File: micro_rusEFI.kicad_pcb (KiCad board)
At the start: 2 copper layers, 80.6 x 93.7 mm, 172 parts, among them J1 USB_B_Micro, J19 Conn_01x06, J2 Conn_02x05_Odd_Even, J7 TC2030, SW1 SW_Push, SW2 SW_Push, SW3 SW_Push, SW4 SW_Push, U1 STM32F427VGT6, U2 LMR14020, U3 molex_48pin_MRE, U35 MCP6004, U36 MCP6004, U46 MCP6004, U5 LM1117-3.3, U8 MCP6004, X1 8MHz 20pF, Y2 32768 Hz

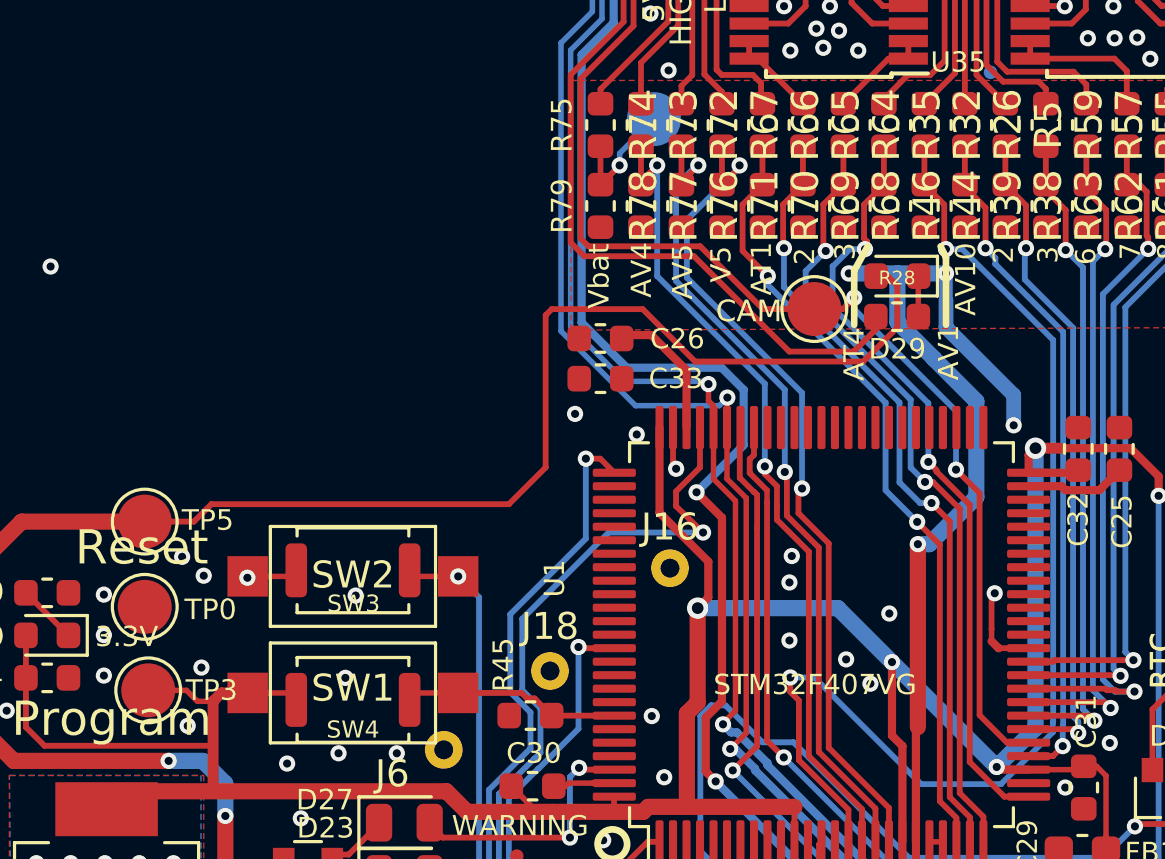
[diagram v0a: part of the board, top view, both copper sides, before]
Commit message: Added CAN x2
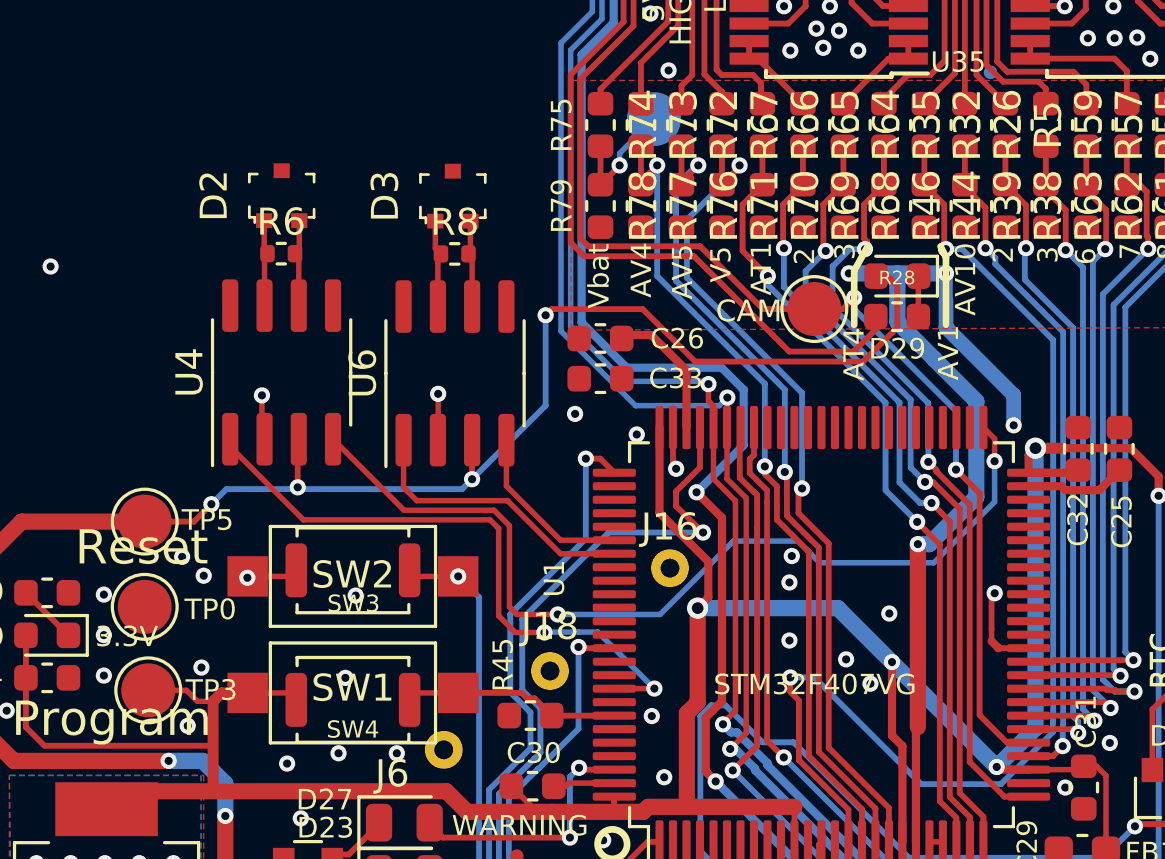
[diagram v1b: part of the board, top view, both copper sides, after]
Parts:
- added D2: PESD1CAN-UX, digikey-footprints:SOT-323, F.Cu at (34.1, 70.0)
- added D3: PESD1CAN-UX, digikey-footprints:SOT-323, F.Cu at (40.4, 70.0)
- added R6: 120, Resistor_SMD:R_0402_1005Metric, F.Cu at (34.1, 72.2)
- added R8: 120, Resistor_SMD:R_0402_1005Metric, F.Cu at (40.5, 72.2)
- added U4: TJA1051T-3, Package_SO:SOIC-8_3.9x4.9mm_P1.27mm, F.Cu at (34.1, 76.6)
- added U6: TJA1051T-3, Package_SO:SOIC-8_3.9x4.9mm_P1.27mm, F.Cu at (40.5, 76.6)
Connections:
- U1 pad 51: /MCU/PB12 -> /CAN Transceiver/RXDCAN1
- U1 pad 81: /MCU/PD0 -> /CAN Transceiver/RXDCAN2
- U1 pad 82: /MCU/PD1 -> /CAN Transceiver/TXDCAN2
- U1 pad 92: /MCU/PB6 -> /CAN Transceiver/TXDCAN1
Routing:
- net /CAN Transceiver/RXDCAN1: track 0.00 -> 34.3 mm, vias 0 -> 2
- net /CAN Transceiver/TXDCAN1: track 0.00 -> 23.1 mm, vias 0 -> 2
- net /CAN Transceiver/TXDCAN2: track 0.00 -> 10.6 mm
- net /CAN Transceiver/RXDCAN2: track 0.00 -> 6.53 mm
- net GND: track 116.4 -> 119.9 mm, vias 234 -> 236
- net Net-(D3-Pad1): track 0.00 -> 3.30 mm
- net Net-(D2-Pad2): track 0.00 -> 3.27 mm
- net Net-(D3-Pad2): track 0.00 -> 3.25 mm
- net Net-(D2-Pad1): track 0.00 -> 3.25 mm
- net /5V: track 335.4 -> 337.3 mm, vias 14 -> 18

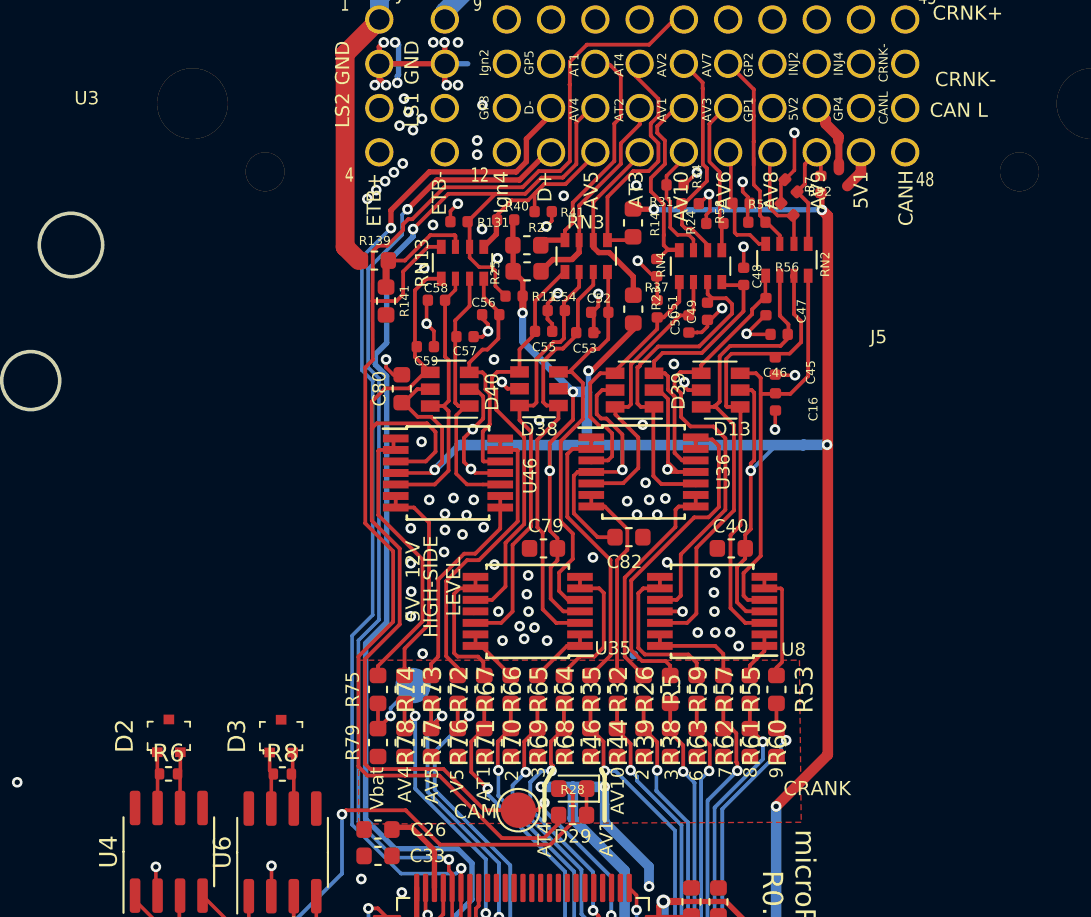
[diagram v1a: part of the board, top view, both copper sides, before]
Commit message: Converted to 4 layer
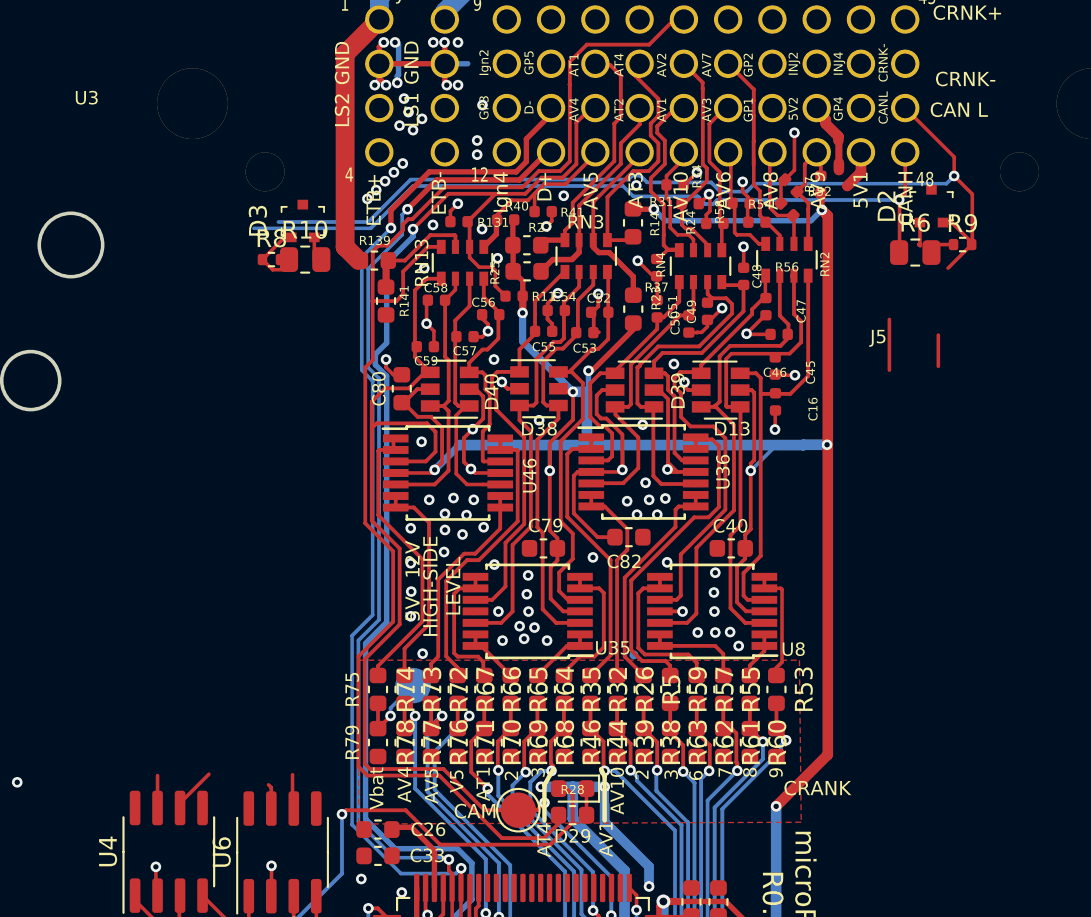
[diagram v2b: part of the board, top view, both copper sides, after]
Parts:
- added R10: 120, Resistor_SMD:R_0805_2012Metric, F.Cu at (41.8, 43.1)
- added R9: 0, Resistor_SMD:R_0402_1005Metric, F.Cu at (78.9, 42.3)
- R6: footprint Resistor_SMD:R_0402_1005Metric -> Resistor_SMD:R_0805_2012Metric
- R8: value 120 -> 0
- moved D2 52.4 mm to (77.2, 40.1)
- moved R6 51.4 mm to (76.2, 42.7)
- moved D3 29.1 mm to (41.7, 40.9)
- moved R8 29.1 mm to (39.9, 43.1)
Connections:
- 10u1 pad 2: /5V -> /TLE8888-1QK/5V
- C6 pad 1: /5V -> /TLE8888-1QK/5V
- C7 pad 1: /5V -> /TLE8888-1QK/5V
- C8 pad 1: /5V -> /TLE8888-1QK/5V
- D2 pad 2: Net-(D2-Pad2) -> Net-(U4-Pad6)
- D3 pad 2: Net-(D3-Pad2) -> Net-(U6-Pad6)
- R4 pad 1: /5V -> /TLE8888-1QK/5V
- R6 pad 1: Net-(D2-Pad1) -> /CANH
- R6 pad 2: Net-(D2-Pad2) -> Net-(R6-Pad2)
- R8 pad 2: Net-(D3-Pad2) -> Net-(R8-Pad2)
- U1 pad 51: /CAN Transceiver/RXDCAN1 -> /MCU/PB12
- U1 pad 81: /CAN Transceiver/RXDCAN2 -> /MCU/PD0
- U1 pad 82: /CAN Transceiver/TXDCAN2 -> /MCU/PD1
- U1 pad 92: /CAN Transceiver/TXDCAN1 -> /MCU/PB6
- U4 pad 3: /5V -> /CAN Transceiver/5V
- U4 pad 6: Net-(D2-Pad2) -> Net-(U4-Pad6)
- U6 pad 3: /5V -> /CAN Transceiver/5V
- U6 pad 6: Net-(D3-Pad2) -> Net-(U6-Pad6)
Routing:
- net /CANL: track 0.00 -> 52.1 mm, vias 0 -> 1
- net /CANH: track 0.00 -> 47.5 mm, vias 0 -> 1
- net /MCU/PB12: track 0.00 -> 34.3 mm, vias 0 -> 2
- net /CAN Transceiver/RXDCAN1: track 34.3 -> 0.00 mm, vias 2 -> 0
- net /MCU/PB6: track 0.00 -> 23.1 mm, vias 0 -> 2
- net /CAN Transceiver/TXDCAN1: track 23.1 -> 0.00 mm, vias 2 -> 0
- net Net-(U4-Pad6): track 0.00 -> 4.79 mm
- net Net-(D2-Pad2): track 3.27 -> 0.00 mm
- net Net-(D3-Pad2): track 3.25 -> 0.00 mm
- net Net-(U6-Pad6): track 0.00 -> 3.20 mm
- net Net-(D3-Pad1): track 3.30 -> 6.24 mm
- net Net-(R6-Pad2): track 0.00 -> 0.88 mm
- net /5V: track 337.3 -> 337.8 mm
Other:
- copper layers 2 -> 4

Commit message: CAN complete
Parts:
- moved R10 1.91 mm to (42.0, 45.0)
- moved R8 1.28 mm to (39.7, 44.4), turned to -90 degrees
- moved R9 0.93 mm to (79.3, 41.4), turned to 90 degrees
- moved D3 0.76 mm to (41.8, 41.7)
- moved R6 0.75 mm to (77.0, 42.7)
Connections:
- 10u1 pad 2: /TLE8888-1QK/5V -> /5V
- C6 pad 1: /TLE8888-1QK/5V -> /5V
- C7 pad 1: /TLE8888-1QK/5V -> /5V
- C8 pad 1: /TLE8888-1QK/5V -> /5V
- D2 pad 1: Net-(D2-Pad1) -> /CANH
- D2 pad 2: Net-(U4-Pad6) -> /CANL
- D3 pad 1: Net-(D3-Pad1) -> /CANL2
- D3 pad 2: Net-(U6-Pad6) -> /CANH2
- R10 pad 2: Net-(U6-Pad6) -> /CANH2
- R4 pad 1: /TLE8888-1QK/5V -> /5V
- R8 pad 1: Net-(D3-Pad1) -> /CANL2
- U3 pad 4: unconnected-(U3-Pad4) -> /CANL2
- U3 pad 8: unconnected-(U3-Pad8) -> /CANH2
- U4 pad 3: /CAN Transceiver/5V -> /5V
- U4 pad 5: /CAN Transceiver/VCC -> /VDD
- U4 pad 6: Net-(U4-Pad6) -> /CANH
- U4 pad 7: Net-(D2-Pad1) -> /CANL
- U6 pad 3: /CAN Transceiver/5V -> /5V
- U6 pad 5: /CAN Transceiver/VCC -> /VDD
- U6 pad 6: Net-(U6-Pad6) -> /CANH2
- U6 pad 7: Net-(D3-Pad1) -> /CANL2
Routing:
- net /CANL2: track 0.00 -> 45.3 mm, vias 0 -> 1
- net /CANH2: track 0.00 -> 43.8 mm, vias 0 -> 1
- net /CANL: track 52.1 -> 85.8 mm, vias 1 -> 2
- net /CANH: track 47.5 -> 79.4 mm, vias 1 -> 2
- net /VDD: track 193.8 -> 214.5 mm, vias 29 -> 36
- net /5V: track 337.8 -> 320.7 mm, vias 18 -> 20
- net /5V2: track 4.02 -> 14.5 mm
- net /5V1: track 2.23 -> 12.6 mm
- net GND: track 119.9 -> 130.0 mm, vias 236 -> 238
- net Net-(D3-Pad1): track 6.24 -> 0.00 mm
- net Net-(U4-Pad6): track 4.79 -> 0.00 mm
- net Net-(D2-Pad1): track 3.21 -> 0.00 mm
- net Net-(U6-Pad6): track 3.20 -> 0.00 mm
- net /CAM_MCU: track 71.2 -> 69.0 mm
- net Net-(R8-Pad2): track 0.00 -> 1.46 mm
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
